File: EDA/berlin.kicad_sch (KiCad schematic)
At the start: 615 parts, among them SW1,1 Rotary_Encoder_Switch_Chassis, SW1,10 MXSwitch, SW1,11 MXSwitch, SW1,12 MXSwitch, SW1,13 MXSwitch, SW1,14 MXSwitch, SW1,15 MXSwitch, SW1,16 Rotary_Encoder_Switch_Chassis, SW1,2 MXSwitch, SW1,3 MXSwitch, SW1,4 MXSwitch, SW1,5 MXSwitch, SW1,6 MXSwitch, SW1,7 MXSwitch, SW1,8 MXSwitch, SW1,9 MXSwitch, SW2,1 MXSwitch, SW2,10 MXSwitch, SW2,11 MXSwitch, SW2,12 MXSwitch, SW2,13 MXSwitch, SW2,14 MXSwitch, SW2,15 MXSwitch, SW2,16 MXSwitch, SW2,17 MXSwitch, SW2,18 MXSwitch, SW2,19 MXSwitch, SW2,2 MXSwitch, SW2,3 MXSwitch, SW2,4 MXSwitch, SW2,5 MXSwitch, SW2,6 MXSwitch, SW2,7 MXSwitch, SW2,9 MXSwitch, SW20-7,3 MXSwitch, SW3,1 MXSwitch, SW3,10 MXSwitch, SW3,11 MXSwitch, SW3,12 MXSwitch, SW3,13 MXSwitch, SW3,14 MXSwitch, SW3,15 MXSwitch, SW3,16 MXSwitch, SW3,17 MXSwitch, SW3,18 MXSwitch, SW3,19 MXSwitch, SW3,2 MXSwitch, SW3,3 MXSwitch, SW3,4 MXSwitch, SW3,5 MXSwitch, SW3,6 MXSwitch, SW3,7 MXSwitch, SW3,8 MXSwitch, SW3,9 MXSwitch, SW39-7,6 MXSwitch, SW4,1 MXSwitch, SW4,10 MXSwitch, SW4,11 MXSwitch, SW4,12 MXSwitch, SW4,13 MXSwitch, SW4,14 MXSwitch, SW4,15 MXSwitch, SW4,16 MXSwitch, SW4,17 MXSwitch, SW4,18 MXSwitch, SW4,19 MXSwitch, SW4,2 MXSwitch, SW4,3 MXSwitch, SW4,4 MXSwitch, SW4,5 MXSwitch, SW4,6 MXSwitch, SW4,7 MXSwitch, SW4,8 MXSwitch, SW4,9 MXSwitch, SW5,1 MXSwitch, SW5,10 MXSwitch, SW5,11 MXSwitch, SW5,12 MXSwitch, SW5,13 MXSwitch, SW5,14 MXSwitch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

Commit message: add some pcb design best practices
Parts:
- renumbered SW7,18 to SW7,17, SW7,19 to SW7,18
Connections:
- net Col18: now also SW7,18.1 (Col)
- net Col19: no longer SW7,18.1 (Col)
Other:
- moved on the sheet: D?, SW7,18
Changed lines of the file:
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@@
   (junction (at 657.86 171.45) (diameter 0.3048) (color 0 0 0 0))
   (junction (at 657.86 199.39) (diameter 0.3048) (color 0 0 0 0))
+  (junction (at 657.86 227.33) (diameter 0) (color 0 0 0 0))
   (junction (at 669.29 85.09) (diameter 0) (color 0 0 0 0))
   (junction (at 669.29 124.46) (diameter 0.3048) (color 0 0 0 0))
@@
   (junction (at 687.07 171.45) (diameter 0.3048) (color 0 0 0 0))
   (junction (at 687.07 199.39) (diameter 0.3048) (color 0 0 0 0))
-  (junction (at 687.07 227.33) (diameter 0.3048) (color 0 0 0 0))
   (junction (at 687.07 355.6) (diameter 0.3048) (color 0 0 0 0))
   (junction (at 689.61 358.14) (diameter 0.3048) (color 0 0 0 0))
@@
     (stroke (width 0) (type solid) (color 0 0 0 0))
   )
-  (wire (pts (xy 640.08 237.49) (xy 698.5 237.49))
+  (wire (pts (xy 640.08 237.49) (xy 669.29 237.49))
     (stroke (width 0) (type solid) (color 0 0 0 0))
   )
@@
     (stroke (width 0) (type solid) (color 0 0 0 0))
   )
+  (wire (pts (xy 657.86 256.54) (xy 657.86 227.33))
+    (stroke (width 0) (type solid) (color 0 0 0 0))
+  )
   (wire (pts (xy 660.4 143.51) (xy 657.86 143.51))
     (stroke (width 0) (type solid) (color 0 0 0 0))
@@
     (stroke (width 0) (type solid) (color 0 0 0 0))
   )
+  (wire (pts (xy 660.4 256.54) (xy 657.86 256.54))
+    (stroke (width 0) (type solid) (color 0 0 0 0))
+  )
   (wire (pts (xy 669.29 85.09) (xy 669.29 86.36))
     (stroke (width 0) (type solid) (color 0 0 0 0))
@@
     (stroke (width 0) (type solid) (color 0 0 0 0))
   )
+  (wire (pts (xy 669.29 237.49) (xy 669.29 240.03))
+    (stroke (width 0) (type solid) (color 0 0 0 0))
+  )
   (wire (pts (xy 687.07 53.34) (xy 687.07 102.87))
     (stroke (width 0) (type solid) (color 0 0 0 0))
@@
     (stroke (width 0) (type solid) (color 0 0 0 0))
   )
-  (wire (pts (xy 687.07 256.54) (xy 687.07 227.33))
-    (stroke (width 0) (type solid) (color 0 0 0 0))
-  )
   (wire (pts (xy 687.07 355.6) (xy 698.5 355.6))
     (stroke (width 0) (type solid) (color 0 0 0 0))
@@
     (stroke (width 0) (type solid) (color 0 0 0 0))
   )
-  (wire (pts (xy 689.61 256.54) (xy 687.07 256.54))
-    (stroke (width 0) (type solid) (color 0 0 0 0))
-  )
   (wire (pts (xy 689.61 358.14) (xy 698.5 358.14))
     (stroke (width 0) (type solid) (color 0 0 0 0))
@@
     (stroke (width 0) (type solid) (color 0 0 0 0))
   )
-  (wire (pts (xy 698.5 237.49) (xy 698.5 240.03))
-    (stroke (width 0) (type solid) (color 0 0 0 0))
-  )
   (wire (pts (xy 706.12 355.6) (xy 708.66 355.6))
     (stroke (width 0) (type solid) (color 0 0 0 0))
@@
     (effects (font (size 1.27 1.27)) (justify left bottom))
   )
+  (text "." (at 668.02 261.62 0)
+    (effects (font (size 1.27 1.27)) (justify left bottom))
+  )
   (text "+" (at 669.29 107.95 0)
     (effects (font (size 1.27 1.27)) (justify left bottom))
@@
     (effects (font (size 1.27 1.27)) (justify left bottom))
   )
-  (text "." (at 697.23 261.62 0)
-    (effects (font (size 1.27 1.27)) (justify left bottom))
-  )
   (text "Microcontroller" (at 732.79 518.795 180)
     (effects (font (size 3.175 3.175)) (justify right bottom))
@@
     (pin "2")
   )
+  (symbol (lib_id "Diode:1N4148") (at 669.29 243.84 270) (unit 1)
+    (in_bom yes) (on_board yes)
+    (property "Reference" "D?" (id 0) (at 671.2966 242.6716 90)
+      (effects (font (size 1.27 1.27)) (justify left))
+    )
+    (property "Value" "1N4148" (id 1) (at 671.2966 244.983 90)
+      (effects (font (size 1.27 1.27)) (justify left))
+    )
+    (property "Footprint" "acheronComponents:D_SOD-123" (id 2) (at 664.845 243.84 0)
+      (effects (font (size 1.27 1.27)) hide)
+    )
+    (property "Datasheet" "https://assets.nexperia.com/documents/data-sheet/1N4148_1N4448.pdf" (id 3) (at 669.29 243.84 0)
+      (effects (font (size 1.27 1.27)) hide)
+    )
+    (pin "1")
+    (pin "2")
+  )
   (symbol (lib_id "Diode:1N4148") (at 698.5 90.17 270) (unit 1)
     (in_bom yes) (on_board yes)
@@
     (pin "2")
   )
-  (symbol (lib_id "Diode:1N4148") (at 698.5 243.84 270) (unit 1)
-    (in_bom yes) (on_board yes)
-    (property "Reference" "D?" (id 0) (at 700.5066 242.6716 90)
-      (effects (font (size 1.27 1.27)) (justify left))
-    )
-    (property "Value" "1N4148" (id 1) (at 700.5066 244.983 90)
-      (effects (font (size 1.27 1.27)) (justify left))
-    )
-    (property "Footprint" "acheronComponents:D_SOD-123" (id 2) (at 694.055 243.84 0)
-      (effects (font (size 1.27 1.27)) hide)
-    )
-    (property "Datasheet" "https://assets.nexperia.com/documents/data-sheet/1N4148_1N4448.pdf" (id 3) (at 698.5 243.84 0)
-      (effects (font (size 1.27 1.27)) hide)
-    )
-    (pin "1")
-    (pin "2")
-  )
   (symbol (lib_id "Diode:1N4148") (at 1115.06 144.78 180) (unit 1)
     (in_bom yes) (on_board yes)
@@
   (symbol (lib_id "Boston-keyboard-rescue:MXSwitch-Acheron") (at 640.08 256.54 0) (unit 1)
     (in_bom yes) (on_board yes)
-    (property "Reference" "SW7,18" (id 0) (at 636.27 254 0)
+    (property "Reference" "SW7,17" (id 0) (at 636.27 254 0)
       (effects (font (size 1.27 1.27)) (justify left))
     )
@@
     (pin "2")
   )
+  (symbol (lib_id "Boston-keyboard-rescue:MXSwitch-Acheron") (at 669.29 256.54 0) (unit 1)
+    (in_bom yes) (on_board yes)
+    (property "Reference" "SW7,18" (id 0) (at 668.02 255.27 0)
+      (effects (font (size 1.27 1.27)) (justify left))
+    )
+    (property "Value" "MXSwitch" (id 1) (at 665.48 257.81 0)
+      (effects (font (size 0.9906 0.9906)) (justify left))
+    )
+    (property "Footprint" "acheron_MX:MX100" (id 2) (at 669.29 256.54 0)
+      (effects (font (size 1.27 1.27)) hide)
+    )
+    (property "Datasheet" "" (id 3) (at 669.29 256.54 0)
+      (effects (font (size 1.27 1.27)) hide)
+    )
+    (pin "1")
+    (pin "2")
+  )
   (symbol (lib_id "Boston-keyboard-rescue:MXSwitch-Acheron") (at 698.5 102.87 0) (unit 1)
     (in_bom yes) (on_board yes)
@@
     (pin "2")
   )
-  (symbol (lib_id "Boston-keyboard-rescue:MXSwitch-Acheron") (at 698.5 256.54 0) (unit 1)
-    (in_bom yes) (on_board yes)
-    (property "Reference" "SW7,19" (id 0) (at 697.23 255.27 0)
-      (effects (font (size 1.27 1.27)) (justify left))
-    )
-    (property "Value" "MXSwitch" (id 1) (at 694.69 257.81 0)
-      (effects (font (size 0.9906 0.9906)) (justify left))
-    )
-    (property "Footprint" "acheron_MX:MX100" (id 2) (at 698.5 256.54 0)
-      (effects (font (size 1.27 1.27)) hide)
-    )
-    (property "Datasheet" "" (id 3) (at 698.5 256.54 0)
-      (effects (font (size 1.27 1.27)) hide)
-    )
-    (pin "1")
-    (pin "2")
-  )
   (symbol (lib_id "LED:NeoPixel_THT") (at 133.35 497.205 0) (unit 1)
     (in_bom yes) (on_board yes)
@@
     )
     (path "/39f60b34-a995-46c9-8c7d-261924a0b227"
-      (reference "SW7,18") (unit 1) (value "MXSwitch") (footprint "acheron_MX:MX200")
+      (reference "SW7,17") (unit 1) (value "MXSwitch") (footprint "acheron_MX:MX200")
     )
     (path "/09c4c891-fcc6-42c3-9a68-6e258f1a0174"
-      (reference "SW7,19") (unit 1) (value "MXSwitch") (footprint "acheron_MX:MX100")
+      (reference "SW7,18") (unit 1) (value "MXSwitch") (footprint "acheron_MX:MX100")
     )
     (path "/2d4acf07-bb42-4d25-a4d7-901ca5970456"

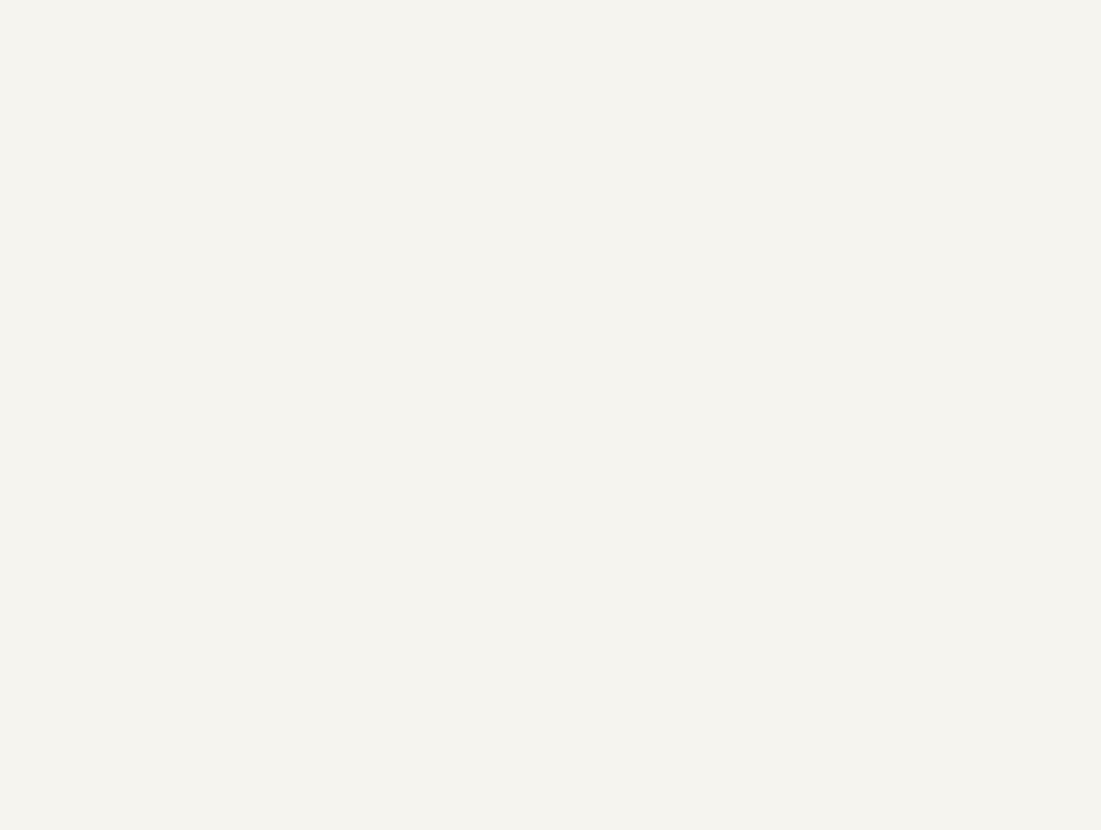
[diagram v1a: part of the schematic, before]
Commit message: add stlink library and symbol
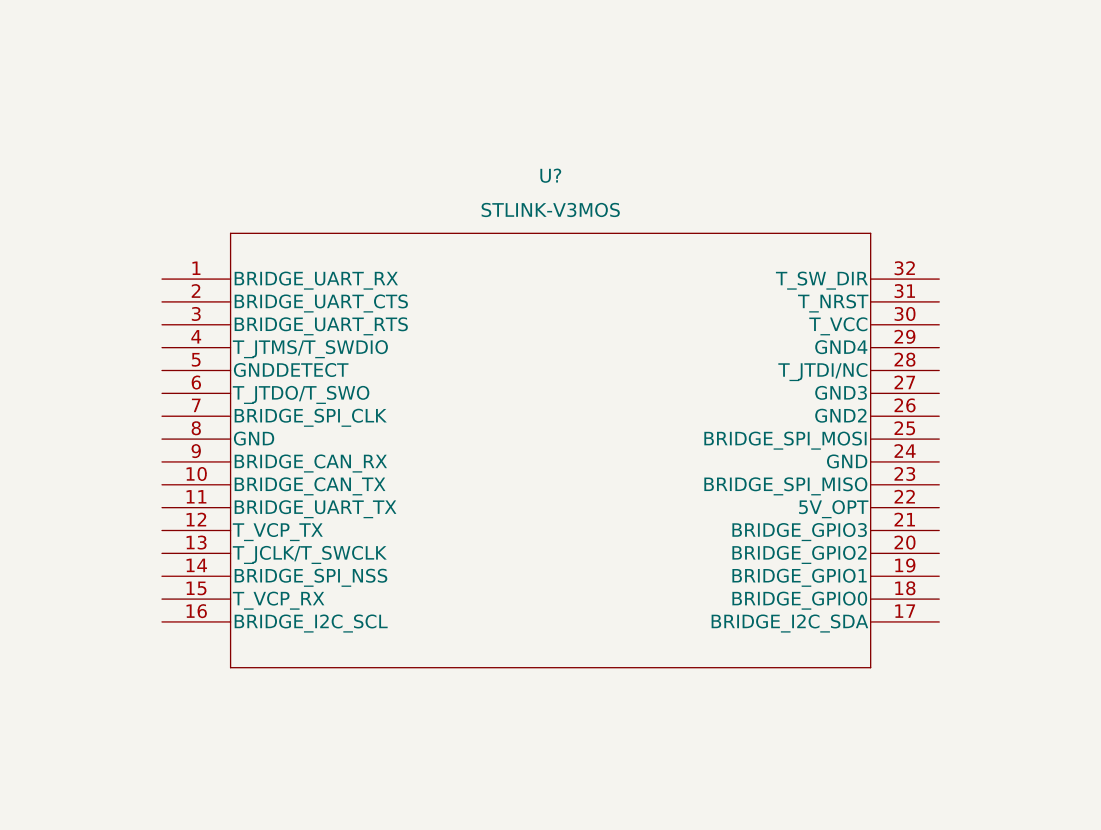
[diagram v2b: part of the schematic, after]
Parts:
- added U?: STLINK-V3MOS, mod_stlink-v3m_mb1467, symbol 2021-09-10_10-17-26:STLINK-V3MOS
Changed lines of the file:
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@@
+    (pin "9")
+  )
+  (symbol (lib_id "2021-09-10_10-17-26:STLINK-V3MOS") (at 988.06 229.87 0) (unit 1)
+    (in_bom yes) (on_board yes) (fields_autoplaced)
+    (property "Reference" "U?" (id 0) (at 1031.24 218.44 0)
+      (effects (font (size 1.524 1.524)))
+    )
+    (property "Value" "STLINK-V3MOS" (id 1) (at 1031.24 222.25 0)
+      (effects (font (size 1.524 1.524)))
+    )
+    (property "Footprint" "mod_stlink-v3m_mb1467" (id 2) (at 1031.24 223.774 0)
+      (effects (font (size 1.524 1.524)) hide)
+    )
+    (property "Datasheet" "" (id 3) (at 988.06 229.87 0)
+      (effects (font (size 1.524 1.524)))
+    )
+    (pin "1")
+    (pin "10")
+    (pin "11")
+    (pin "12")
+    (pin "13")
+    (pin "14")
+    (pin "15")
+    (pin "16")
+    (pin "17")
+    (pin "18")
+    (pin "19")
+    (pin "2")
+    (pin "20")
+    (pin "21")
+    (pin "22")
+    (pin "23")
+    (pin "24")
+    (pin "25")
+    (pin "26")
+    (pin "27")
+    (pin "28")
+    (pin "29")
+    (pin "3")
+    (pin "30")
+    (pin "31")
+    (pin "32")
+    (pin "4")
+    (pin "5")
+    (pin "6")
+    (pin "7")
+    (pin "8")
     (pin "9")
   )
@@
       (reference "U?") (unit 1) (value "STM32F072CBTx") (footprint "Package_QFP:LQFP-48_7x7mm_P0.5mm")
     )
+    (path "/8803122e-1b6e-4571-81bc-a3b1f9eb73ab"
+      (reference "U?") (unit 1) (value "STLINK-V3MOS") (footprint "mod_stlink-v3m_mb1467")
+    )
     (path "/b10b63ef-46f2-4433-8852-57de5d0f3d2e"

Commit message: route first usb/kb nets
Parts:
- removed U?: STLINK-V3MOS, mod_stlink-v3m_mb1467, symbol 2021-09-10_10-17-26:STLINK-V3MOS
- gave numbers to parts that had none: 2
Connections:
- net Col7: now also U?.78 (PC10)
- net Col8: now also U?.77 (PA15)
- net Col9: now also U?.89 (PB3)
- net Row1: now also U?.90 (PB4)
- net Row2: now also U?.91 (PB5)
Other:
- moved on the sheet: C?, D?, J?, Q?, R?, SW?, U?

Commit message: more routing
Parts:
- gave numbers to parts that had none: 1
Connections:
- net Col1: now also U1001.65 (PC8)
- net Col10: now also U1001.51 (PB12)
- net Col2: now also U1001.66 (PC9)
- net Col3: now also U1001.67 (PA8)
- net Col4: now also U1001.68 (PA9)
- net Col5: now also U1001.69 (PA10)
- net Col6: now also U1001.64 (PC7)
- net Row3: now also U1001.52 (PB13)
- net Row4: now also U1001.53 (PB14)
- net Row5: now also U1001.54 (PB15)
- net Row6: now also U1001.63 (PC6)
